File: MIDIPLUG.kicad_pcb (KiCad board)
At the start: 4 copper layers, 24.4 x 31.1 mm, 31 parts, among them J1 Joystick Port, P1 LINE OUT, U1 LP2985-3.3, U2 SAM2695, Y1 12Mhz

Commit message: Change gnd plane
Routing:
- net GND: track 107.6 -> 114.5 mm, vias 12 -> 13
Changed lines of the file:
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@@
     (thickness 1.6)
     (drawings 25)
-    (tracks 283)
+    (tracks 287)
     (zones 0)
     (modules 31)
@@
   (page A4)
   (layers
-    (0 F.Cu signal hide)
-    (1 In1.Cu power hide)
-    (2 In2.Cu power hide)
-    (31 B.Cu signal hide)
+    (0 F.Cu signal)
+    (1 In1.Cu power)
+    (2 In2.Cu power)
+    (31 B.Cu signal)
     (32 B.Adhes user)
     (33 F.Adhes user)
@@
   (segment (start 128.8415 93.7895) (end 126.8095 93.7895) (width 0.2) (layer B.Cu) (net 1))
   (segment (start 123.9935 92.739) (end 126.775 92.739) (width 0.2) (layer B.Cu) (net 1))
+  (via (at 108.204 90.932) (size 0.6) (drill 0.3) (layers F.Cu B.Cu) (net 1))
+  (segment (start 108.204 90.932) (end 113.284 90.932) (width 0.2) (layer In1.Cu) (net 1))
+  (segment (start 113.411 90.805) (end 113.411 89.0905) (width 0.2) (layer In1.Cu) (net 1))
+  (segment (start 113.284 90.932) (end 113.411 90.805) (width 0.2) (layer In1.Cu) (net 1))
   (segment (start 113.647 79.8195) (end 113.8985 79.568) (width 0.2) (layer F.Cu) (net 2))
   (segment (start 113.8985 79.568) (end 114.212102 79.568) (width 0.2) (layer F.Cu) (net 2))

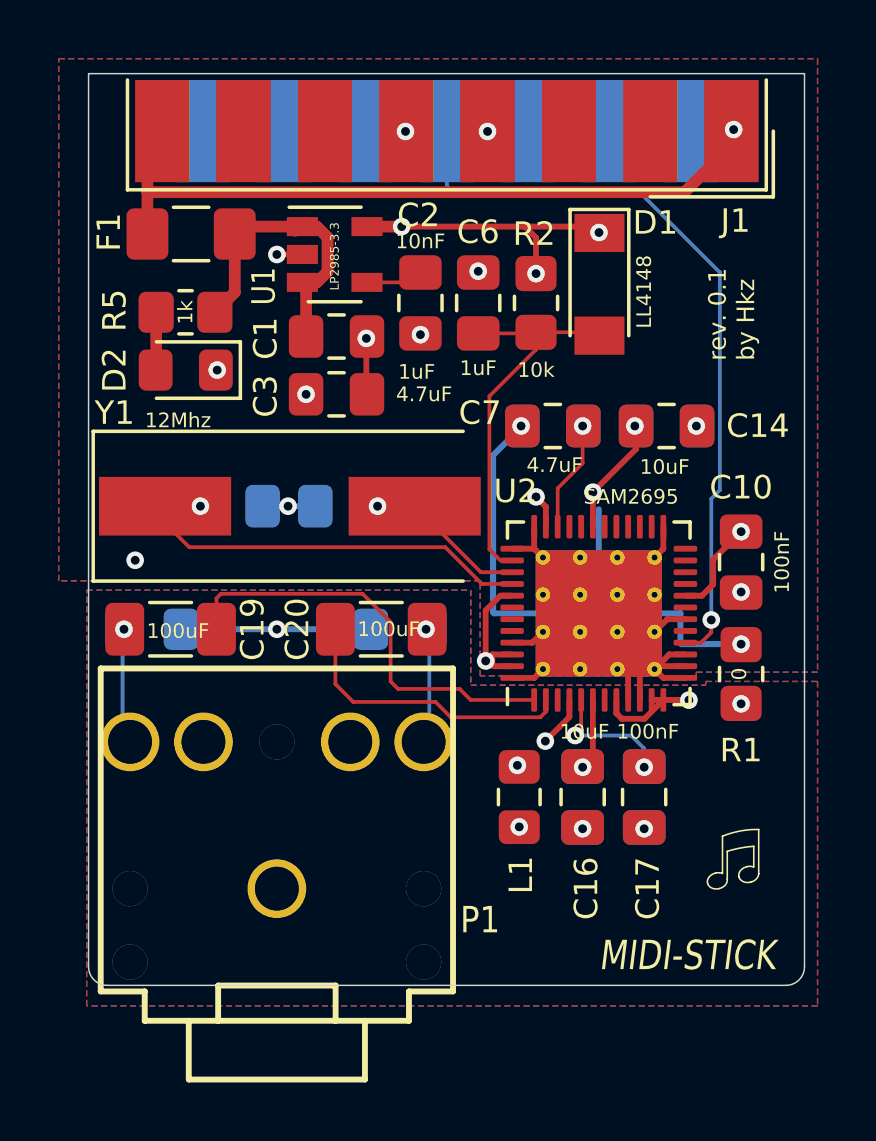
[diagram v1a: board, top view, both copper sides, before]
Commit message: Add hole on underside of SAM chip
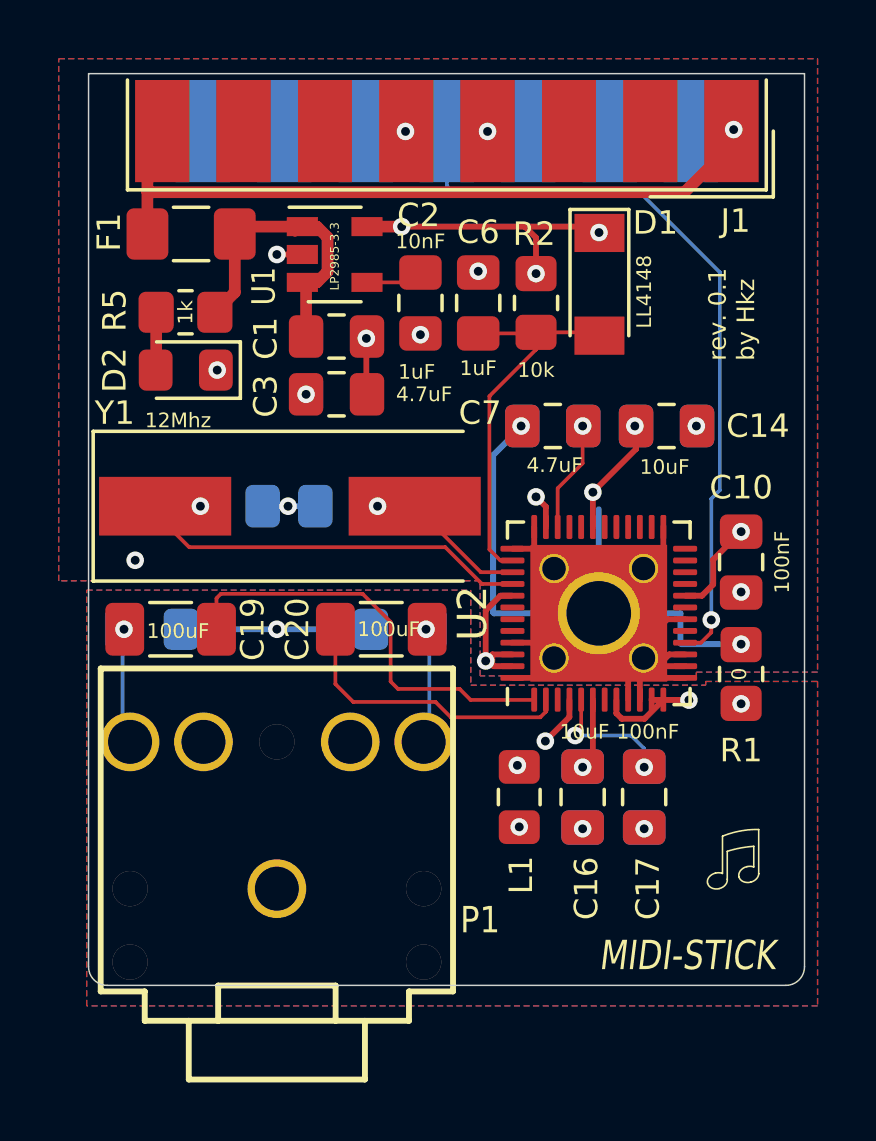
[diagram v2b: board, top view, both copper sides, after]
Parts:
- U2: footprint Package_DFN_QFN:QFN-48-1EP_6x6mm_P0.4mm_EP4.3x4.3mm_ThermalVias -> MIDIPLUG:QFN-48-1EP_6x6mm_P0.4mm_EP4.66x4.66mm_BackHoles
